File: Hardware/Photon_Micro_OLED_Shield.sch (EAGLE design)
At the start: 27 parts

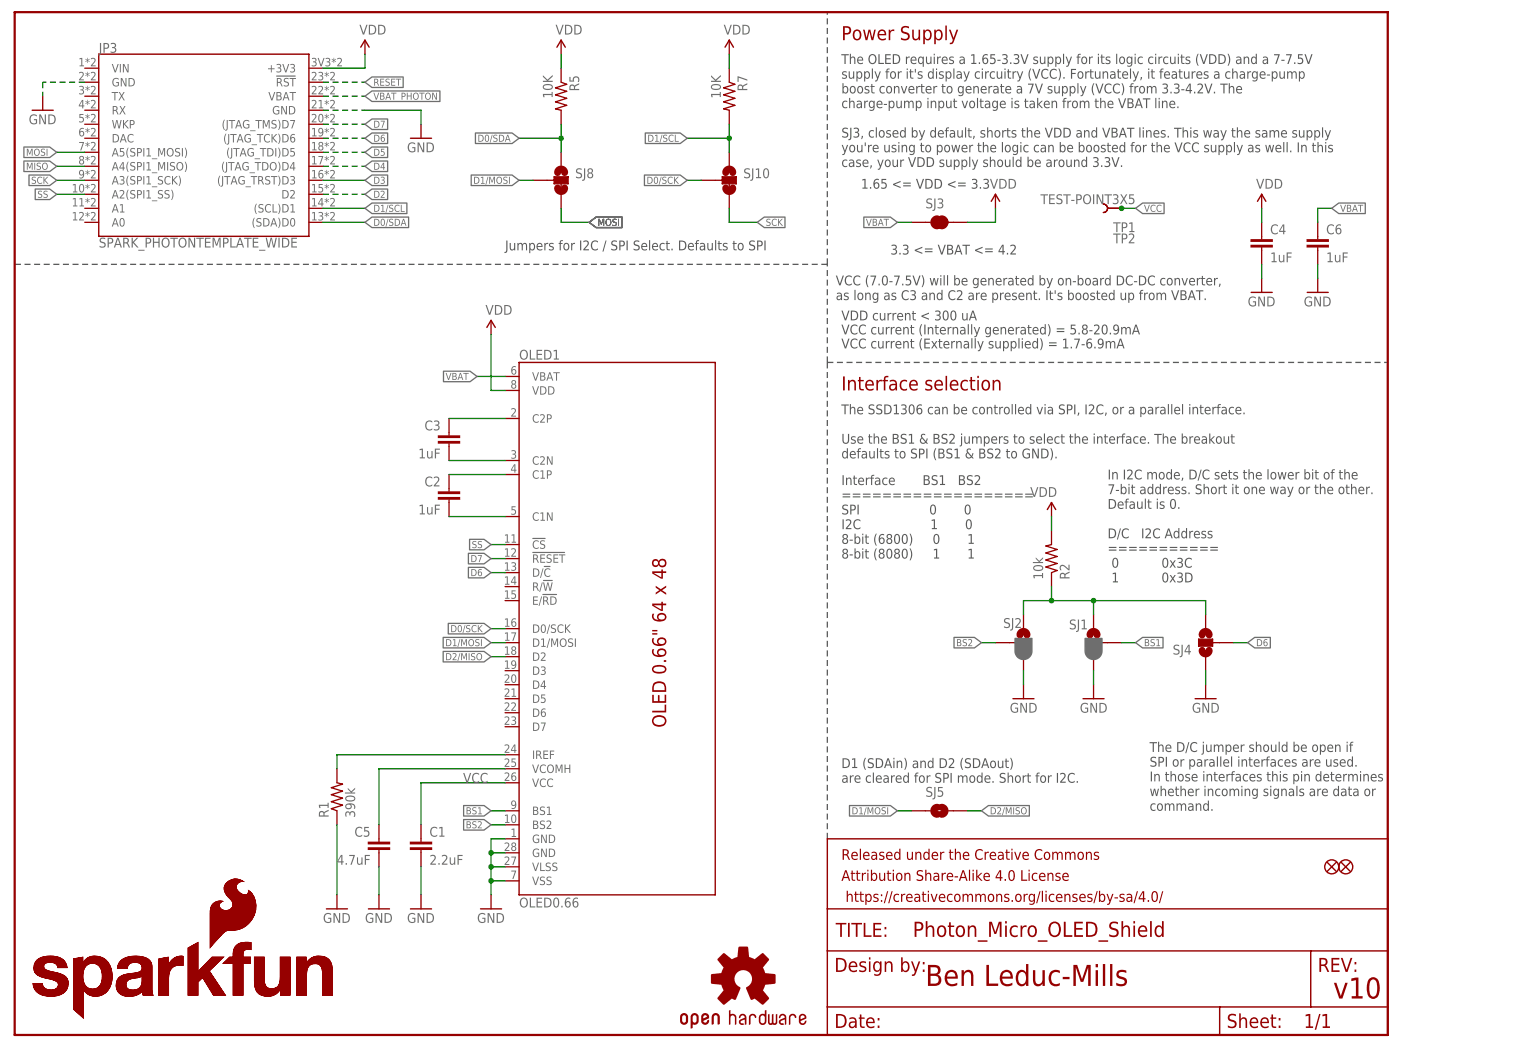
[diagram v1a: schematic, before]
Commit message: Cleaned up the schematic a lot
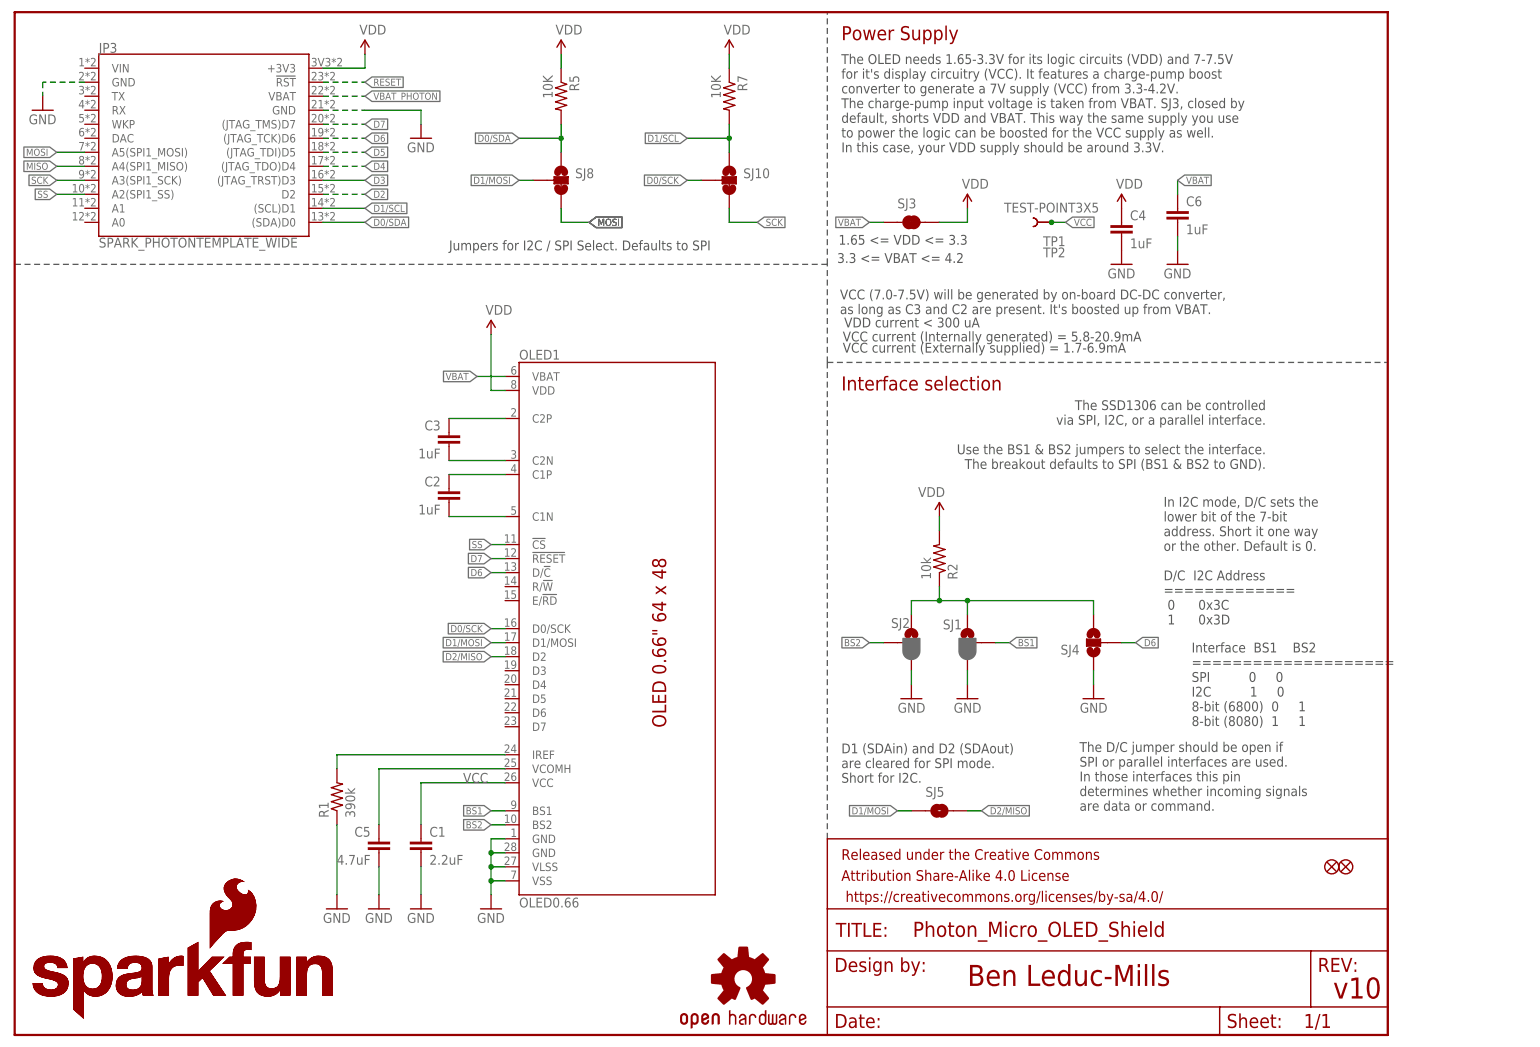
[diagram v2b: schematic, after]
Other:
- note added: "In I2C mode, D/C sets the lower bit of the 7-bit address. Short it one way or the other. Default is 0. D/C I2C Address ============= 0 0x3C 1 0x3D"
- note added: "Interface BS1 BS2 ==================== SPI 0 0 I2C 1 0 8-bit (6800) 0 1 8-bit (8080) 1 1"
- note added: "The OLED needs 1.65-3.3V for its logic circuits (VDD) and 7-7.5V for it's display circuitry (VCC). It features a charge-pump boost converter to generate a 7V supply (VCC) from 3.3-4.2V. The charge-pump input voltage is taken from VBAT. SJ3, closed by default, shorts VDD and VBAT. This way the same supply you use to power the logic can be boosted for the VCC supply as well. In this case, your VDD 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"
- note removed: "In I2C mode, D/C sets the lower bit of the 7-bit address. Short it one way or the other. Default is 0. D/C I2C Address =========== 0 0x3C 1 0x3D"
- note removed: "Interface BS1 BS2 =================== SPI 0 0 I2C 1 0 8-bit (6800) 0 1 8-bit (8080) 1 1"
- note removed: "The OLED requires a 1.65-3.3V supply for its logic circuits (VDD) and a 7-7.5V supply for it's display circuitry (VCC). Fortunately, it features a charge-pump boost converter to generate a 7V supply (VCC) from 3.3-4.2V. The charge-pump input voltage is taken from the VBAT line. SJ3, closed by default, shorts the VDD and VBAT lines. This way the same supply you're using to power the logic can be b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"
- moved on the sheet: C4, C6, R2, SJ1, SJ2, SJ3, SJ4, TP1, TP2
